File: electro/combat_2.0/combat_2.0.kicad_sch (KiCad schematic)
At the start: 9 parts

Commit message: PCB V0
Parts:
- removed F?: 12A, symbol Device:Polyfuse_Small
- C1, C2: renamed from C?; footprint (none) -> Capacitor_SMD:C_0805_2012Metric
- F1: renamed from F?; footprint (none) -> Capacitor_THT:C_Rect_L13.0mm_W3.0mm_P10.00mm_FKS3_FKP3_MKS4
- J1: renamed from J?; footprint (none) -> TerminalBlock:TerminalBlock_Altech_AK300-2_P5.00mm
- U1: renamed from U?; footprint (none) -> ESP8266:ESP12F-Devkit-V3
- gave numbers to parts that had none: 3
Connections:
- net +3V3: now also U1.25 (3.3V)
- net GND: now also J1.1 (Pin_1), U1.10 (GND), U1.17 (GND), U1.24 (GND); no longer J1.2 (Pin_2)
- net IN_B_1: now also U1.23 (D5(GPIO14)); no longer U1.26 (D4(GPIO2))
- net IN_B_2: now also U1.22 (D6(GPIO12)); no longer U1.23 (D5(GPIO14))
- net IN__A_1: now also U1.27 (D3(GPIO0)); no longer U1.29 (D1(GPIO5))
- net PWM_A: now also U1.29 (D1(GPIO5)); no longer U1.30 (D0(GPIO16))
- net PWM_B: now also U1.21 (D7(GPIO13)); no longer U1.27 (D3(GPIO0))
- net at F1.2: now also J1.2 (Pin_2); no longer J1.1 (Pin_1)
- no-connect marks 0 -> 1
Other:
- sheet weapon_motor ports: added 3.3V; removed none
- moved on the sheet: F1, J1

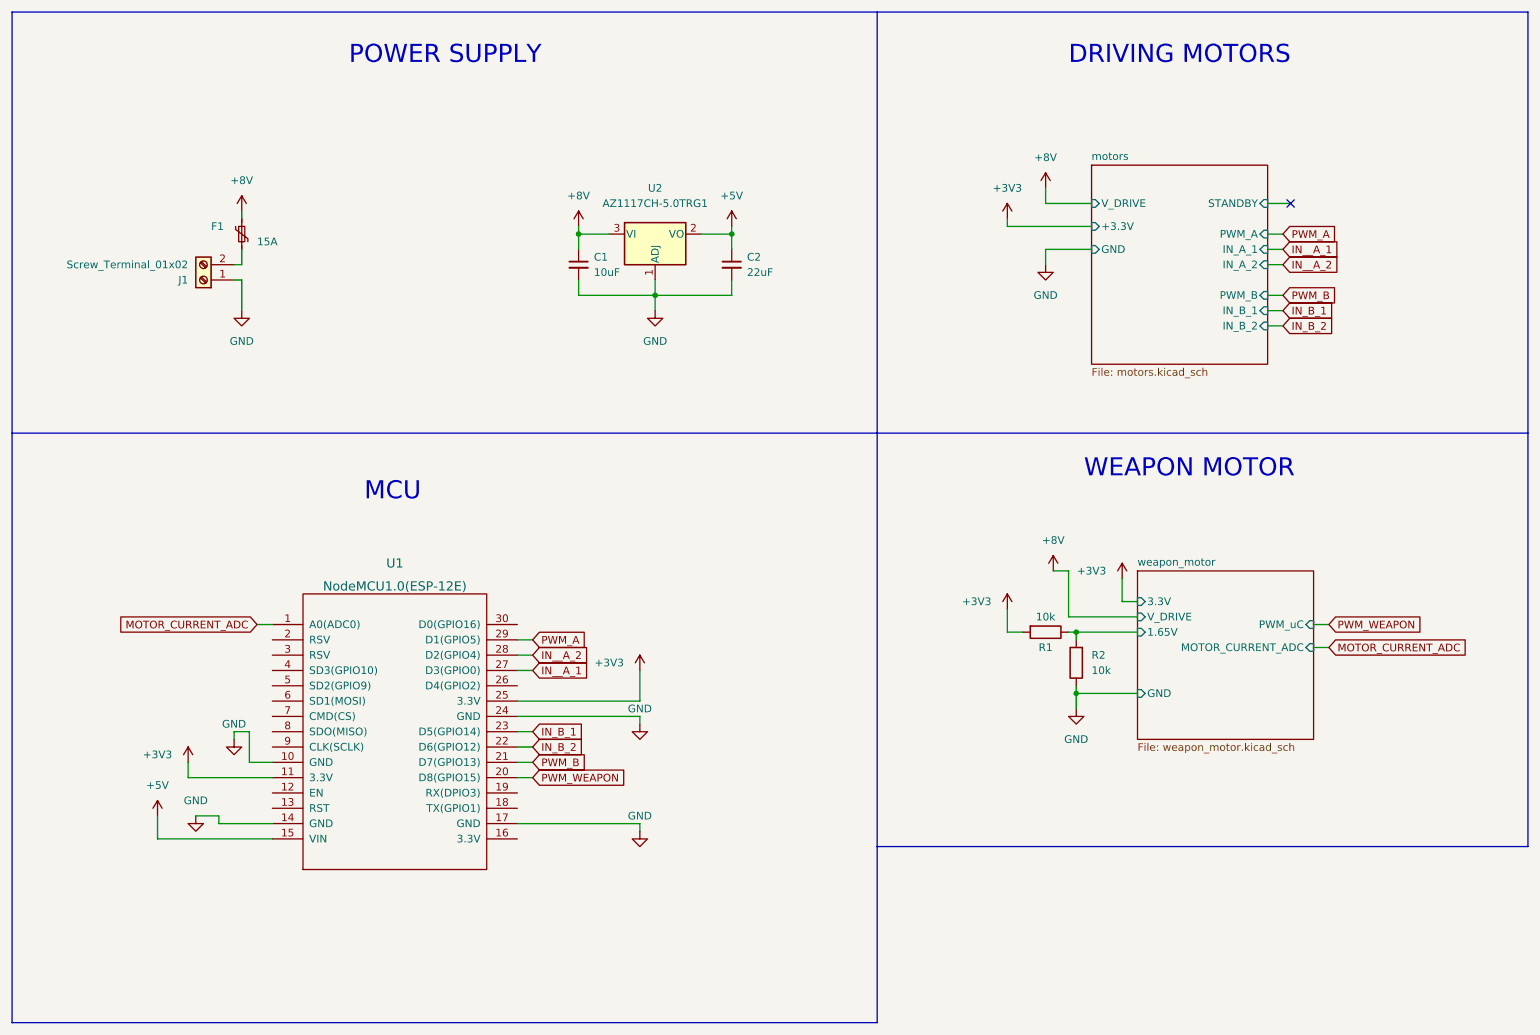
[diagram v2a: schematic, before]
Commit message: Added UART connector and voltage divider for battery volt. measurement
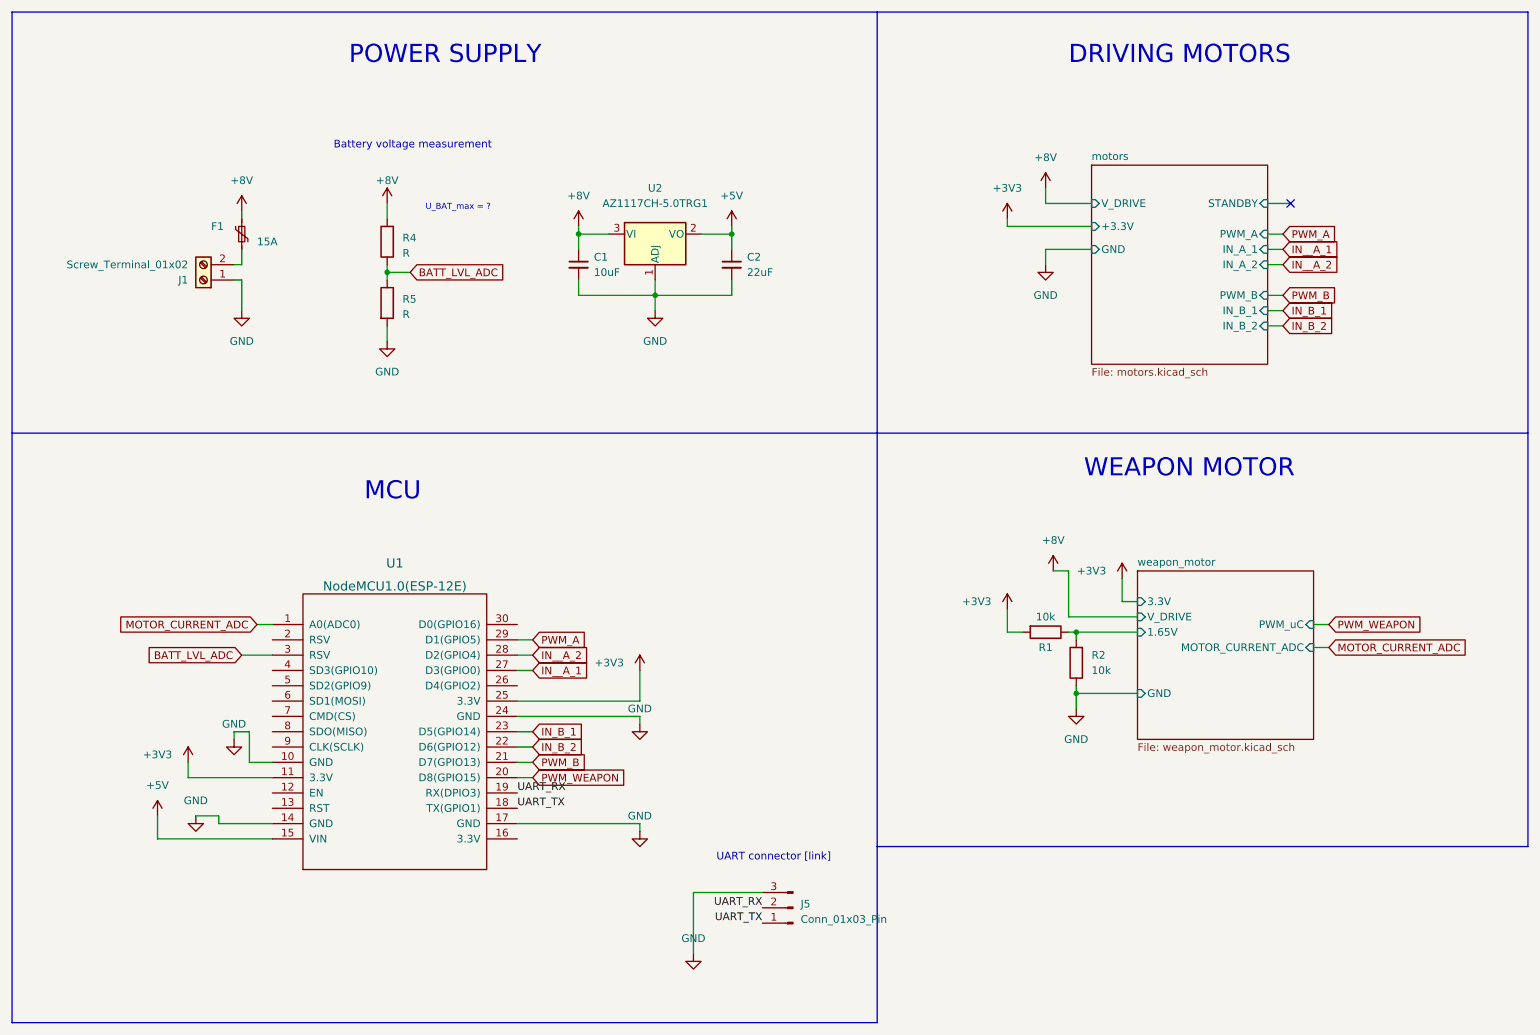
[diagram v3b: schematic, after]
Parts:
- added J5: Conn_01x03_Pin, Connector_PinHeader_2.54mm:PinHeader_1x03_P2.54mm_Vertical, symbol Connector:Conn_01x03_Pin
- added R4, R5: R, symbol Device:R
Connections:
- net +8V: now also R4.2
- net GND: now also J5.3 (Pin_3), R5.2
- net UART_TX: now reaches U1.18 (TX(GPIO1))
- net UART_TX: now also J5.1 (Pin_1)
- net UART_RX: now reaches U1.19 (RX(DPIO3))
- net UART_RX: now also J5.2 (Pin_2)
- net BATT_LVL_ADC: now reaches U1.3 (RSV)
- net BATT_LVL_ADC: now also R4.1, R5.1
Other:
- note added: "Battery voltage measurement"
- note added: "UART connector [link]"
- note added: "U_BAT_max = ?"

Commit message: Standarized schematic labels
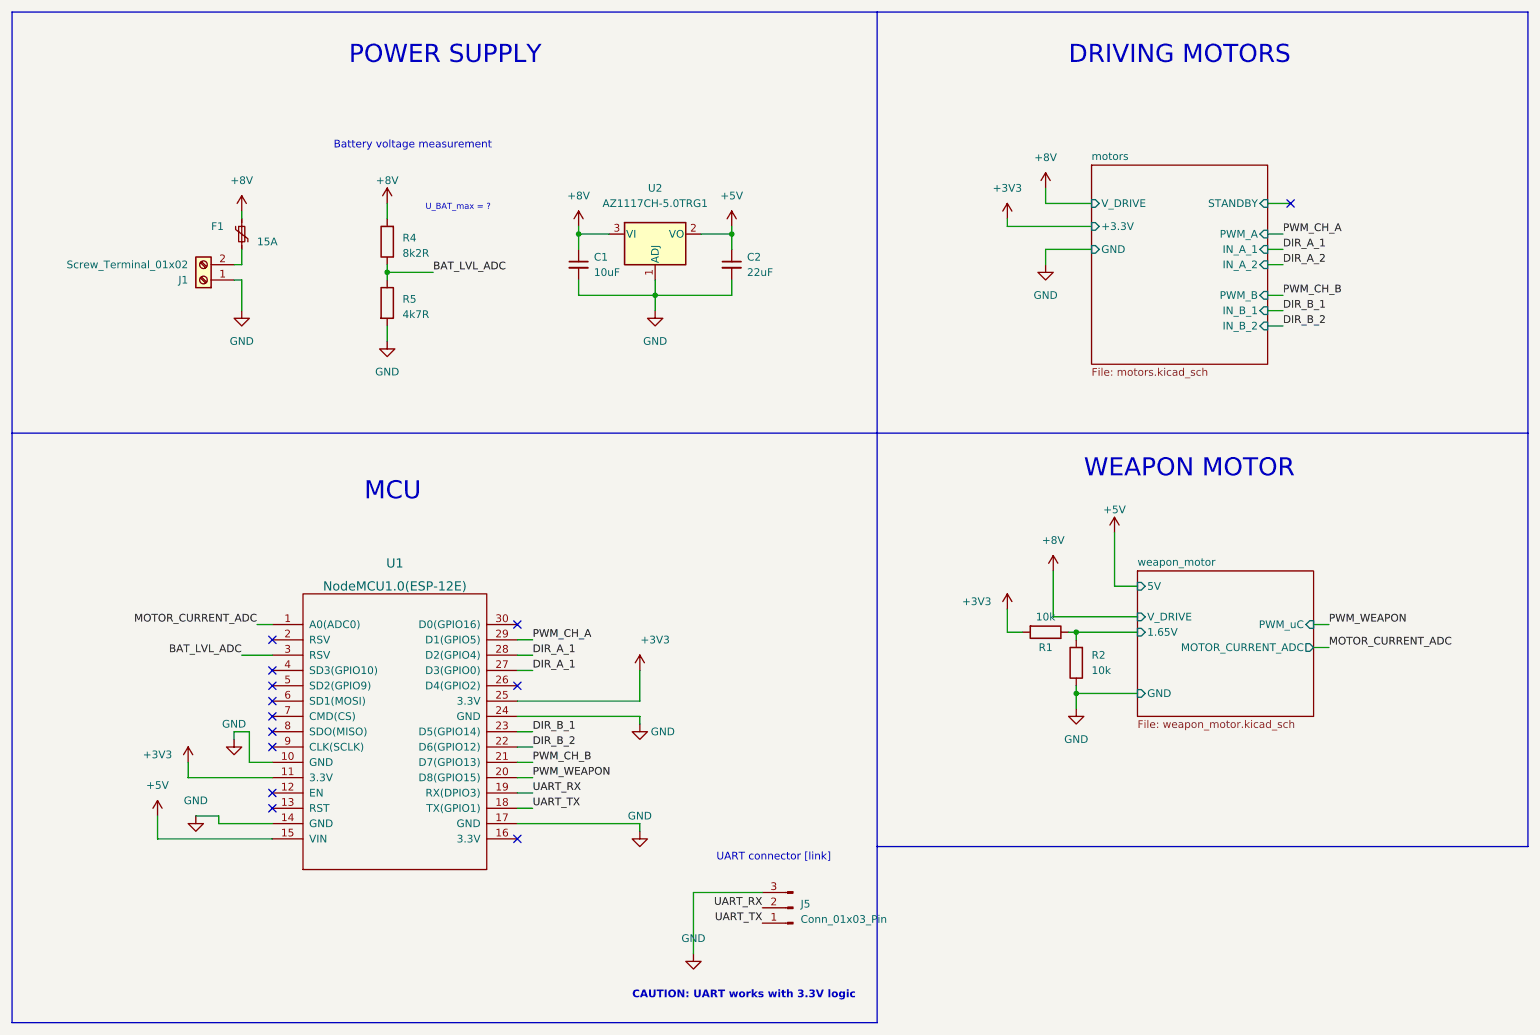
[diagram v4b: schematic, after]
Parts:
- R4: value R -> 8k2R
- R5: value R -> 4k7R
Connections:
- net IN__A_2 is gone; now on net DIR_A_1: U1.28 (D2(GPIO4))
- net BATT_LVL_ADC renamed BAT_LVL_ADC
- net IN_B_1 renamed DIR_B_1
- net IN_B_2 renamed DIR_B_2
- net IN__A_1 renamed DIR_A_1
- net PWM_A renamed PWM_CH_A
- net PWM_B renamed PWM_CH_B
- no-connect marks 1 -> 13
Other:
- sheet weapon_motor ports: added 5V; removed 3.3V
- note added: "CAUTION: UART works with 3.3V logic"

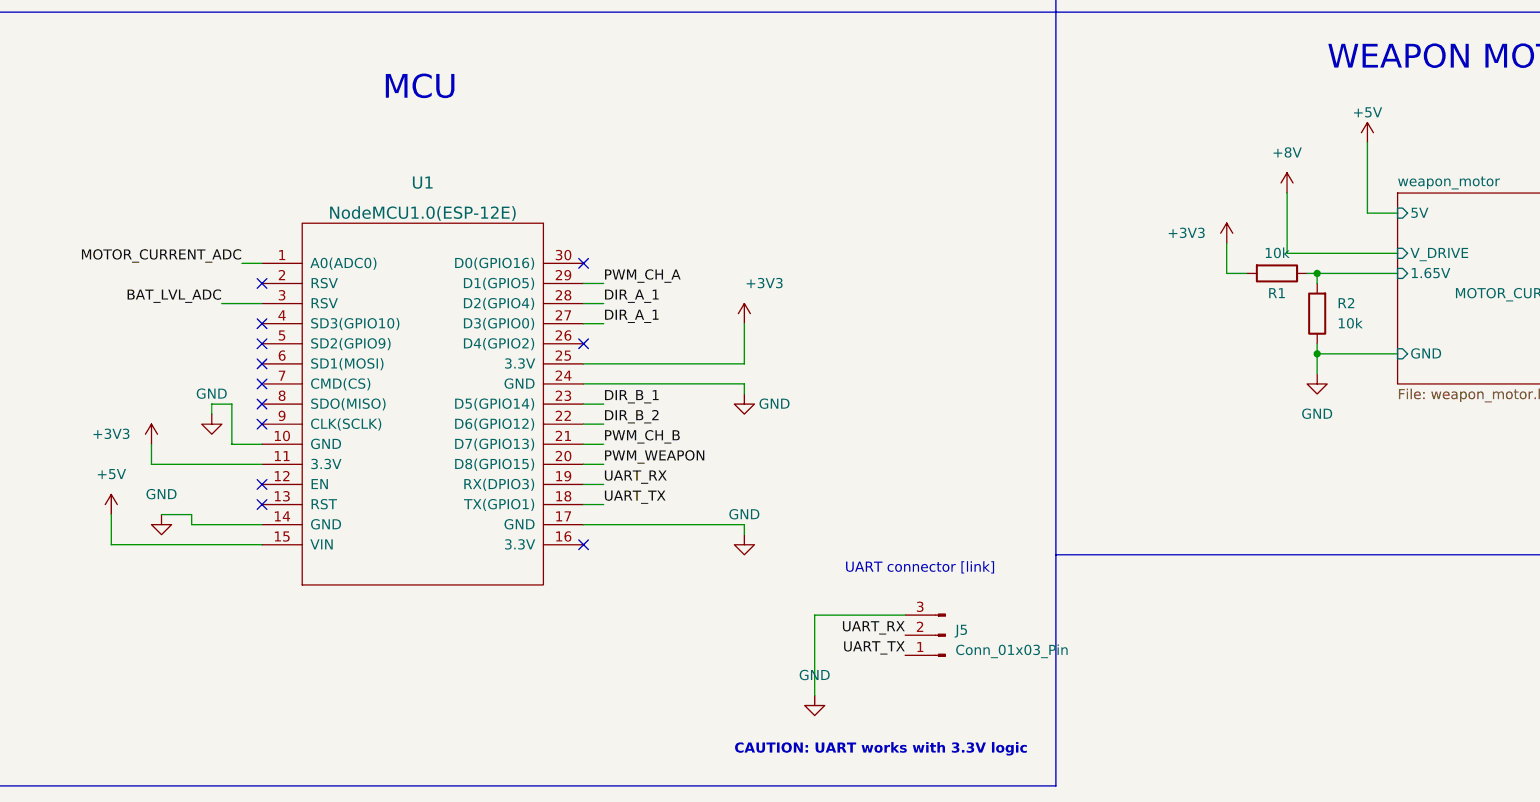
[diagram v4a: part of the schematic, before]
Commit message: Changed resistors to SMD1206 type, hand-soldered version (slightly bigger pads)
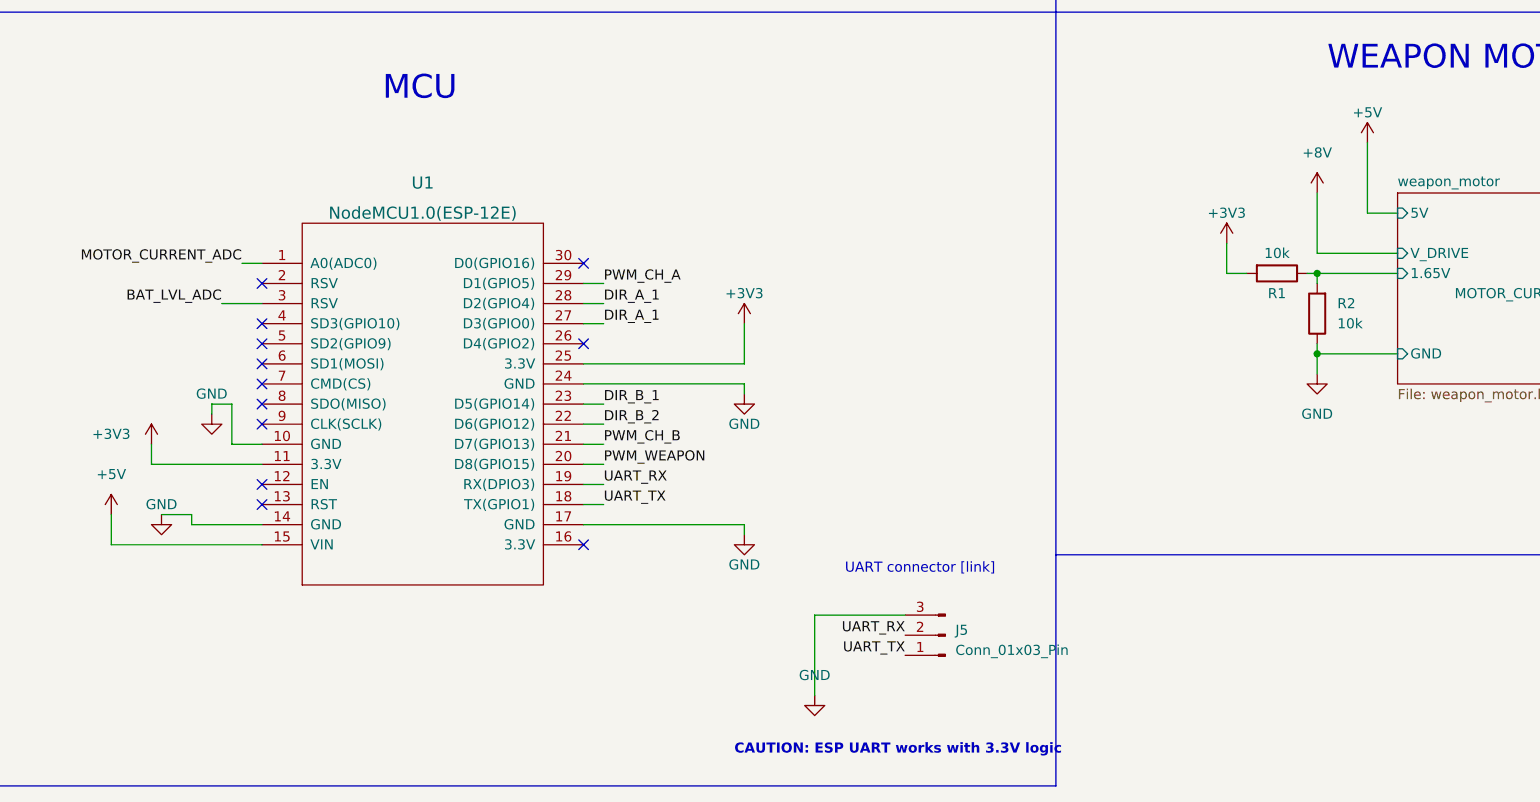
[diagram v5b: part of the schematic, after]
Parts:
- R1, R2, R4, R5: footprint (none) -> Resistor_SMD:R_1206_3216Metric_Pad1.30x1.75mm_HandSolder
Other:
- note added: "CAUTION: ESP UART works with 3.3V logic"
- note removed: "CAUTION: UART works with 3.3V logic"
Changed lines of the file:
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@@
     (stroke (width 0) (type default))
   )
-  (wire (pts (xy 195.58 119.38) (xy 209.55 119.38))
+  (wire (pts (xy 199.39 119.38) (xy 209.55 119.38))
     (stroke (width 0) (type default))
   )
@@
     (stroke (width 0) (type default))
   )
-  (wire (pts (xy 195.58 111.76) (xy 195.58 119.38))
+  (wire (pts (xy 199.39 111.76) (xy 199.39 119.38))
     (stroke (width 0) (type default))
   )
@@
     (effects (font (size 3 3)) (justify left bottom))
   )
-  (text "CAUTION: UART works with 3.3V logic" (at 125.73 182.88 0)
+  (text "CAUTION: ESP UART works with 3.3V logic" (at 125.73 182.88 0)
     (effects (font (size 1.27 1.27) (thickness 0.254) bold (color 204 102 0 1)) (justify left bottom))
   )
@@
       (effects (font (size 1.27 1.27)) (justify left))
     )
-    (property "Footprint" "" (at 83.312 67.31 90)
+    (property "Footprint" "Resistor_SMD:R_1206_3216Metric_Pad1.30x1.75mm_HandSolder" (at 83.312 67.31 90)
       (effects (font (size 1.27 1.27)) hide)
     )
@@
       (effects (font (size 1.27 1.27)) (justify right))
     )
-    (property "Footprint" "" (at 86.868 57.15 90)
+    (property "Footprint" "Resistor_SMD:R_1206_3216Metric_Pad1.30x1.75mm_HandSolder" (at 86.868 57.15 90)
       (effects (font (size 1.27 1.27)) hide)
     )
@@
     )
   )
-  (symbol (lib_id "power:+8V") (at 195.58 111.76 0) (unit 1)
-    (in_bom yes) (on_board yes) (dnp no) (fields_autoplaced)
-    (property "Reference" "#PWR014" (at 195.58 115.57 0)
-      (effects (font (size 1.27 1.27)) hide)
-    )
-    (property "Value" "+8V" (at 195.58 106.68 0)
-      (effects (font (size 1.27 1.27)))
-    )
-    (property "Footprint" "" (at 195.58 111.76 0)
-      (effects (font (size 1.27 1.27)) hide)
-    )
-    (property "Datasheet" "" (at 195.58 111.76 0)
+  (symbol (lib_id "power:+8V") (at 199.39 111.76 0) (unit 1)
+    (in_bom yes) (on_board yes) (dnp no) (fields_autoplaced)
+    (property "Reference" "#PWR014" (at 199.39 115.57 0)
+      (effects (font (size 1.27 1.27)) hide)
+    )
+    (property "Value" "+8V" (at 199.39 106.68 0)
+      (effects (font (size 1.27 1.27)))
+    )
+    (property "Footprint" "" (at 199.39 111.76 0)
+      (effects (font (size 1.27 1.27)) hide)
+    )
+    (property "Datasheet" "" (at 199.39 111.76 0)
       (effects (font (size 1.27 1.27)) hide)
     )
@@
       (effects (font (size 1.27 1.27)) hide)
     )
-    (property "Value" "+3V3" (at 129.54 123.19 0)
+    (property "Value" "+3V3" (at 127 124.46 0)
       (effects (font (size 1.27 1.27)))
     )
@@
       (effects (font (size 1.27 1.27)) hide)
     )
-    (property "Value" "GND" (at 130.81 138.43 0)
+    (property "Value" "GND" (at 127 140.97 0)
       (effects (font (size 1.27 1.27)))
     )
@@
       (effects (font (size 1.27 1.27)) hide)
     )
-    (property "Value" "+3V3" (at 182.88 116.84 0)
+    (property "Value" "+3V3" (at 187.96 114.3 0)
       (effects (font (size 1.27 1.27)))
     )
@@
       (effects (font (size 1.27 1.27)) hide)
     )
-    (property "Value" "GND" (at 127 152.4 0)
+    (property "Value" "GND" (at 127 158.75 0)
       (effects (font (size 1.27 1.27)))
     )
@@
       (effects (font (size 1.27 1.27)) (justify right))
     )
-    (property "Footprint" "" (at 201.168 127 90)
+    (property "Footprint" "Resistor_SMD:R_1206_3216Metric_Pad1.30x1.75mm_HandSolder" (at 201.168 127 90)
       (effects (font (size 1.27 1.27)) hide)
     )
@@
       (effects (font (size 1.27 1.27)))
     )
-    (property "Footprint" "" (at 194.31 120.142 90)
+    (property "Footprint" "Resistor_SMD:R_1206_3216Metric_Pad1.30x1.75mm_HandSolder" (at 194.31 120.142 90)
       (effects (font (size 1.27 1.27)) hide)
     )
@@
       (effects (font (size 1.27 1.27)) hide)
     )
-    (property "Value" "GND" (at 53.34 149.86 0)
-      (effects (font (size 1.27 1.27)))
-    )
+    (property "Value" "GND" (at 53.34 151.13 0)
+      (effects (font (size 1.27 1.27)))
+    )
